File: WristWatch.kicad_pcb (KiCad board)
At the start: 4 copper layers, 32 x 32 mm, 86 parts, among them Q1 Q_PMOS_GSD, Q2 Q_PMOS_GSD, U2 STM32L412KBUx, U3 LIS2DE12, U4 AP2205-3.0, U5 MCP73832-2-OT, U6 ESP32-C3, Y1 32.768k

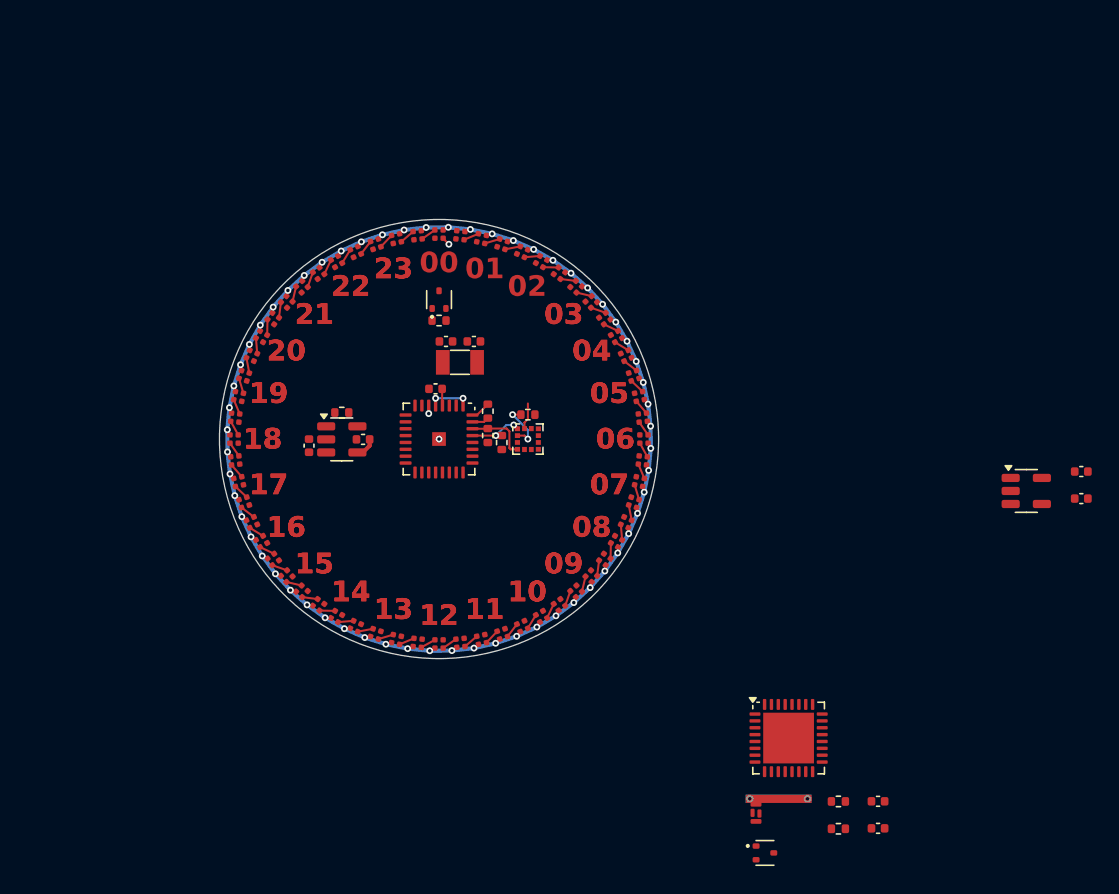
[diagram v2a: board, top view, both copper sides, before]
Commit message: This board is actually stupid. Moving on. Dual MCU architecture felt cool. It was in fact, overly complicated. Finally got the STM32F401 RTC to work. Fighting the L412 though.
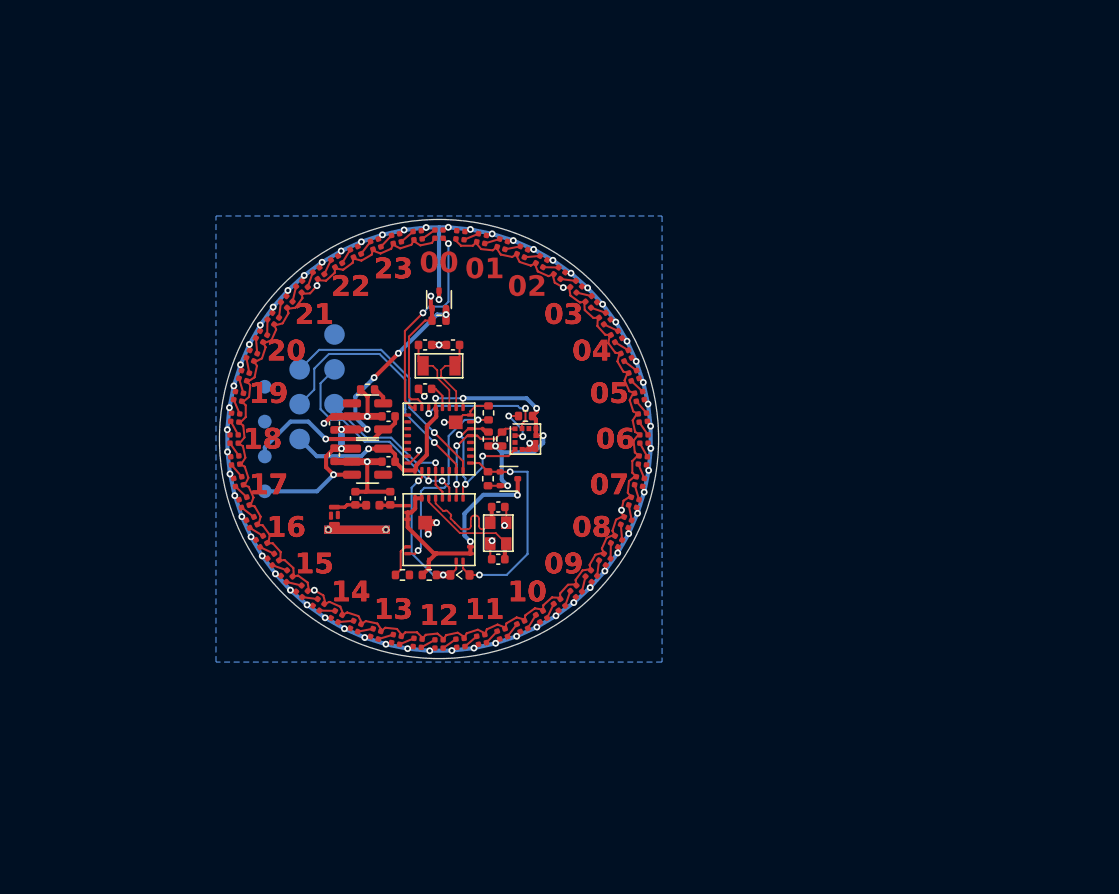
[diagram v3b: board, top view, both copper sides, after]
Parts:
- added C18: 1.8p, Capacitor_SMD:C_0402_1005Metric, F.Cu at (-3.56, 4.32)
- added C19: 1.2p, Capacitor_SMD:C_0402_1005Metric, F.Cu at (-6.10, 4.32)
- added D61: D, Diode_SMD:D_SOD-523, F.Cu at (1.52, 9.91)
- added J1: vcc, TestPoint:TestPoint_Pad_D1.0mm, B.Cu at (-12.7, 3.81)
- added J2: gnd, TestPoint:TestPoint_Pad_D1.0mm, B.Cu at (-12.7, -3.81)
- added J3: vcc, TestPoint:TestPoint_Pad_D1.0mm, B.Cu at (-12.7, 1.27)
- added J4: gnd, TestPoint:TestPoint_Pad_D1.0mm, B.Cu at (-12.7, -1.27)
- added L2: 3n, Inductor_SMD:L_0402_1005Metric, F.Cu at (-4.83, 4.83)
- added R13: 1M, Resistor_SMD:R_0402_1005Metric, F.Cu at (-0.71, 9.91)
- added TP1: ETX_SRX, TestPoint:TestPoint_Pad_D1.5mm, B.Cu at (-7.62, -2.54)
- added TP2: ERX_STX, TestPoint:TestPoint_Pad_D1.5mm, B.Cu at (-7.62, -5.08)
- added TP3: SWDIO, TestPoint:TestPoint_Pad_D1.5mm, B.Cu at (-10.2, -2.54)
- added TP4: SWCLK, TestPoint:TestPoint_Pad_D1.5mm, B.Cu at (-10.2, -5.08)
- added TP5: VCC, TestPoint:TestPoint_Pad_D1.5mm, B.Cu at (-10.2, 0.00)
- added TP6: GND, TestPoint:TestPoint_Pad_D1.5mm, B.Cu at (-7.62, -7.62)
- added Y2: 40M, Crystal:Crystal_SMD_2520-4Pin_2.5x2.0mm, F.Cu at (4.32, 6.86)
- AE1: moved to B.Cu
- moved C12 54.4 mm to (-7.62, 1.14), turned to -90 degrees
- moved C13 50.6 mm to (-3.68, 1.65), turned to 180 degrees
- moved U4 48.1 mm to (-5.21, 1.65)
- moved AE1 38.3 mm to (-7.62, 4.99)
- moved R12 36.8 mm to (-2.67, 9.91)
- moved C16 35.0 mm to (4.32, 4.95), turned to 180 degrees
- moved R11 34.7 mm to (3.57, 2.90), turned to -90 degrees
- moved C17 33.9 mm to (4.32, 8.76)
- moved Q2 33.0 mm to (5.09, 2.90)
- moved U6 29.7 mm to (0.00, 6.60)
- moved R10 2.52 mm to (-5.21, -3.61)
- moved U5 2.52 mm to (-5.21, -1.65)
- moved C14 2.50 mm to (-3.68, -1.65)
- moved C15 2.47 mm to (-7.62, -1.14)
- moved C4 1.55 mm to (1.02, -6.86)
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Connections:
- net Net-(U2-PC14) renamed /stm_xtal+
- net Net-(U2-PC15) renamed /stm_xtal-
- net Net-(U6-XTAL_N) renamed /esp_xtal+
- net Net-(U6-XTAL_P) renamed /esp_xtal-
- C1 pad 1: GND -> Net-(U2-NRST)
- C1 pad 2: Net-(U2-NRST) -> GND
- C12 pad 1: VCC -> +BATT
- Q1 pad 1: Net-(Q1-G) -> LED_PWR_EN
- R1 pad 1: GND -> STM_BOOT
- R1 pad 2: Net-(U2-PH3) -> GND
- R6 pad 1: Net-(Q1-G) -> LED_PWR_EN
- U2 pad 13: LED_IN -> unconnected-(U2-PA7-Pad13)
- U2 pad 18: unconnected-(U2-PA8-Pad18) -> ESP_BOOT
- U2 pad 19: unconnected-(U2-PA9-Pad19) -> ESP_RX
- U2 pad 20: unconnected-(U2-PA10-Pad20) -> ESP_TX
- U2 pad 23: unconnected-(U2-PA13-Pad23) -> SWDIO
- U2 pad 24: unconnected-(U2-PA14-Pad24) -> SWCLK
- U2 pad 25: unconnected-(U2-PA15-Pad25) -> ESP_PWR_EN
- U2 pad 31: Net-(U2-PH3) -> STM_BOOT
- U2 pad 7: unconnected-(U2-PA1-Pad7) -> LED_PWR_EN
- U2 pad 8: unconnected-(U2-PA2-Pad8) -> LED_IN
- U4 pad 1: VCC -> +BATT
- U4 pad 3: VCC -> +BATT
- U6 pad 1: Net-(AE1-A) -> Net-(U6-LNA_IN)
- U6 pad 15: BOOT -> ESP_BOOT
- U6 pad 16: unconnected-(U6-GPIO10-Pad16) -> ESP_PWR_EN
- U6 pad 8: unconnected-(U6-GPIO3-Pad8) -> STM_BOOT
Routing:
- net GND: track 1.45 -> 142.6 mm, vias 1 -> 16
- net +3V0: track 3.07 -> 37.4 mm, vias 2 -> 7
- net +BATT: track 0.00 -> 29.7 mm, vias 0 -> 7
- net /ESP_VDD: track 0.00 -> 19.1 mm, vias 0 -> 2
- net SWDIO: track 0.00 -> 19.0 mm, vias 0 -> 1
- net SWCLK: track 0.00 -> 17.8 mm, vias 0 -> 1
- net ESP_PWR_EN: track 0.00 -> 16.5 mm, vias 0 -> 2
- net ESP_RX: track 0.00 -> 16.3 mm, vias 0 -> 2
- net STM_BOOT: track 0.00 -> 15.0 mm, vias 0 -> 2
- net LED_IN: track 0.61 -> 14.9 mm, vias 1 -> 2
- net ESP_BOOT: track 0.00 -> 12.6 mm, vias 0 -> 2
- net ESP_TX: track 0.00 -> 11.7 mm, vias 0 -> 1
- net VBUS: track 1.55 -> 12.4 mm, vias 0 -> 1
- net LED_PWR_EN: track 0.00 -> 9.85 mm, vias 0 -> 1
- net /esp_xtal-: track 0.00 -> 8.36 mm
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- added copper zone on B.Cu, net GND
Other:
- copper layers 4 -> 2
- board text added: "BATT"
- board text added: "EEAN"
- board text added: "ERX SCK"
- board text added: "ETX DIO"
- board text added: "GND"
- board text added: "VBUS"
- board text added: "VCC"

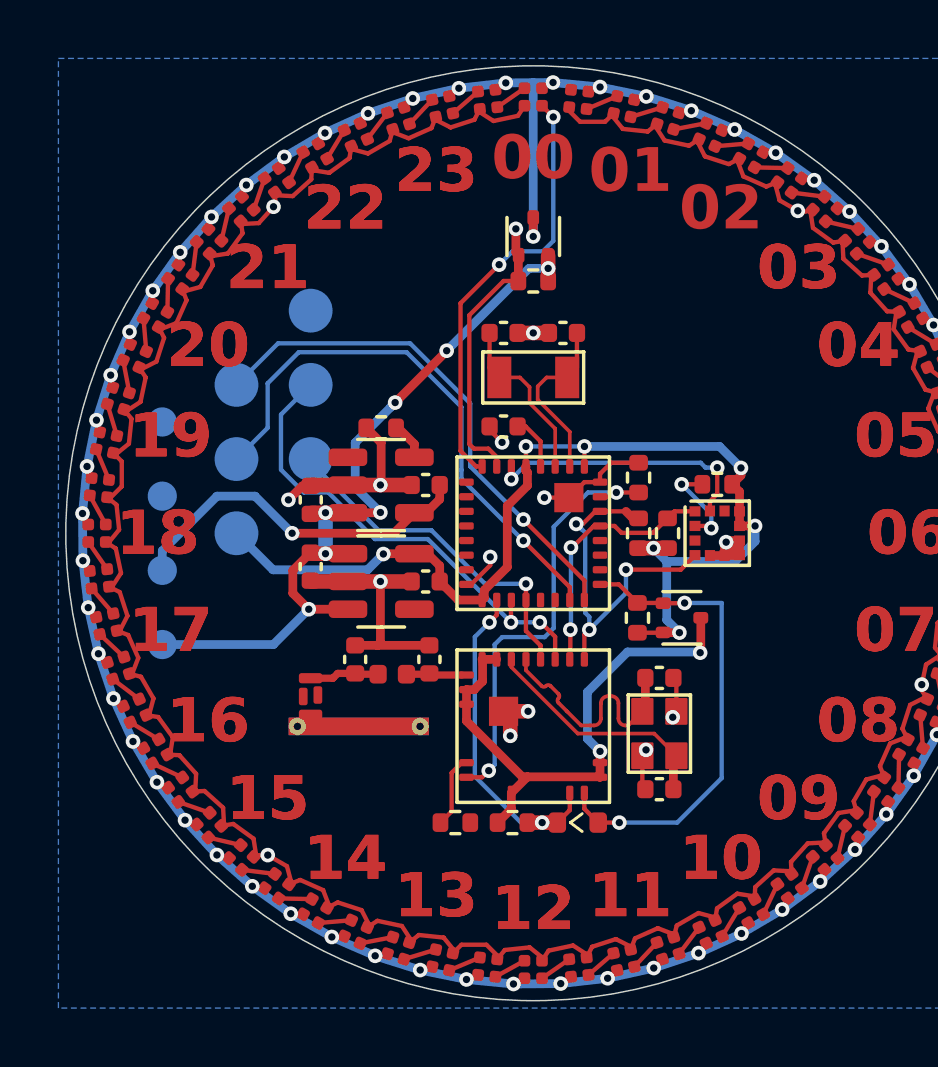
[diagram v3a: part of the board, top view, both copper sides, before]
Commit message: A much more reasonable architecture
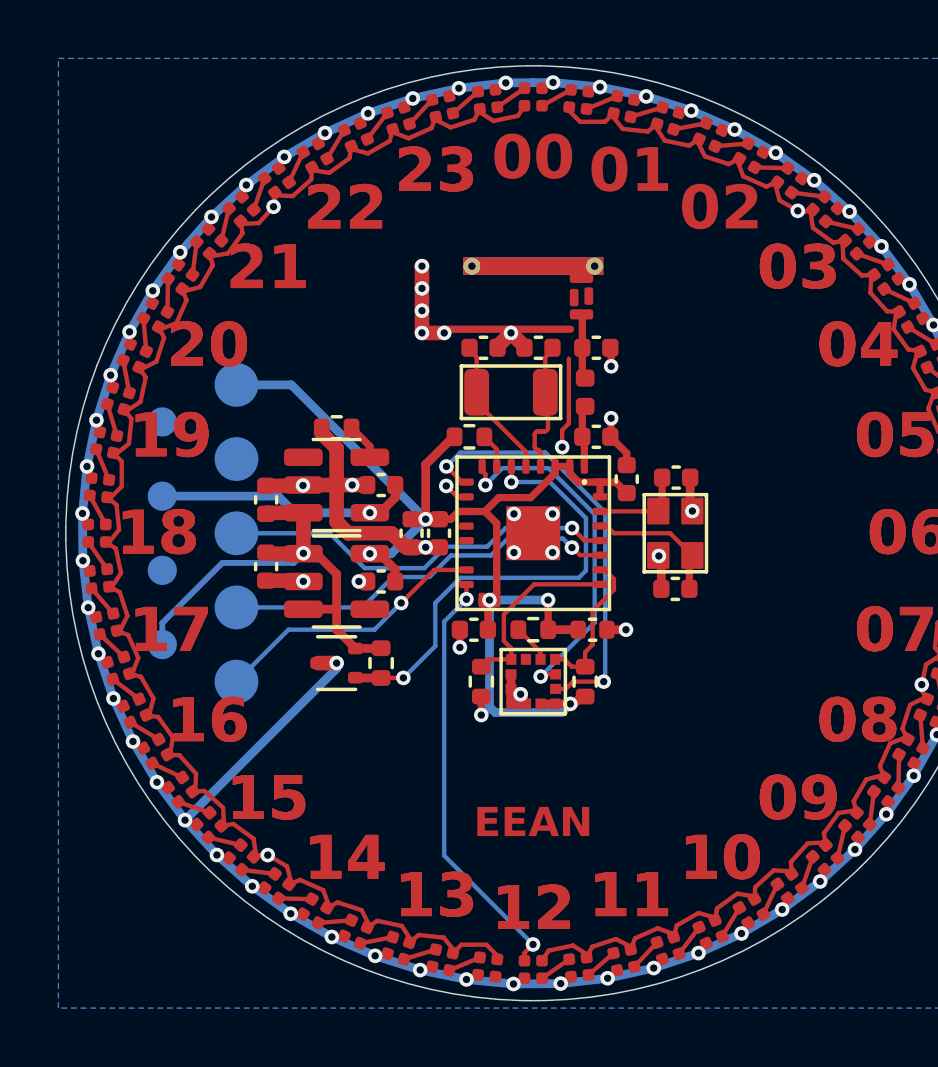
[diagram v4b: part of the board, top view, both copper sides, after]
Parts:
- removed D61: D, Diode_SMD:D_SOD-523
- removed Q2: Q_PMOS_GSD, Package_TO_SOT_SMD:SOT-523
- removed R1: 10k, Resistor_SMD:R_0402_1005Metric
- removed R11, R13: 1M, Resistor_SMD:R_0402_1005Metric
- removed TP4: SWCLK, TestPoint:TestPoint_Pad_D1.5mm
- removed U2: STM32L412KBUx, Package_DFN_QFN:QFN-32-1EP_5x5mm_P0.5mm_EP3.45x3.45mm
- removed Y1: 32.768k, Crystal:Crystal_SMD_3215-2Pin_3.2x1.5mm
- added C20: 100n, Capacitor_SMD:C_0402_1005Metric, F.Cu at (3.20, -1.85)
- added C21: 100n, Capacitor_SMD:C_0402_1005Metric, F.Cu at (-2.03, 3.30)
- added C21: 100n, Capacitor_SMD:C_0402_1005Metric, F.Cu at (2.03, 3.30)
- added C22: 100n, Capacitor_SMD:C_0402_1005Metric, F.Cu at (-3.23, 0.00)
- added Y3: 32.768k, Crystal:Crystal_SMD_EuroQuartz_EQ161-2Pin_3.2x1.5mm, F.Cu at (-0.76, -4.83)
- C1: value 100n -> 12p
- C17: value 12p -> 10u
- C4, C7: value 4p3 -> 12p
- R6: value 1M -> 100k
- TP1: value ETX_SRX -> TX
- TP2: value ERX_STX -> RX
- TP3: value SWDIO -> BOOT
- moved Q1 16.1 mm to (-6.73, 4.45), turned to 180 degrees
- moved AE1 16.1 mm to (0.00, -9.14), turned to 180 degrees
- moved R6 14.1 mm to (-5.21, 4.45), turned to 90 degrees
- moved C19 13.5 mm to (2.16, -6.35), turned to 0 degrees
- moved R12 13.2 mm to (-2.18, -3.30), turned to 180 degrees
- moved C17 12.2 mm to (-4.17, 0.00), turned to -90 degrees
- moved L2 11.7 mm to (1.78, -4.83), turned to 90 degrees
- moved C7 10.6 mm to (4.86, 1.91), turned to 0 degrees
- moved C18 9.52 mm to (2.16, -3.30), turned to 0 degrees
- moved U3 8.09 mm to (0.00, 5.08), turned to -90 degrees
- moved TP2 8.03 mm to (-10.2, 2.54)
- moved R9 8.03 mm to (0.00, 3.30)
- moved TP3 7.62 mm to (-10.2, 5.08)
- moved R8 7.40 mm to (-1.78, 5.08)
- moved C16 6.88 mm to (4.89, -1.91)
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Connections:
- C1 pad 1: Net-(U2-NRST) -> GND
- C1 pad 2: GND -> /xtl_ls+
- C16 pad 2: /esp_xtal+ -> /xtl_hs-
- C17 pad 1: GND -> +3V0
- C17 pad 2: /esp_xtal- -> GND
- C4 pad 2: /stm_xtal+ -> /xtl_ls-
- C7 pad 2: /stm_xtal- -> /xtl_hs+
- D1 pad 4: LED_IN -> Bank1
- D15 pad 2: Bank1 -> Bank2
- D16 pad 4: Bank1 -> Bank2
- D30 pad 2: Bank2 -> unconnected-(D30-DOUT-Pad2)
- D31 pad 4: Bank2 -> LED_DATA
- D60 pad 2: unconnected-(D60-DOUT-Pad2) -> Bank1
- R12 pad 2: /ESP_VDD -> +3V0
- TP3 pad 1: SWDIO -> ESP_BOOT
- U3 pad 11: IMU_INT2 -> IMU_SPAR_INT
- U3 pad 12: WKUP1 -> IMU_MOVE_INT
- U6 pad 11: /ESP_VDD -> +3V0
- U6 pad 16: ESP_PWR_EN -> LED_DATA
- U6 pad 17: /ESP_VDD -> +3V0
- U6 pad 18: /ESP_VDD -> +3V0
- U6 pad 2: /ESP_VDD -> +3V0
- U6 pad 29: /esp_xtal+ -> /xtl_hs+
- U6 pad 3: /ESP_VDD -> +3V0
- U6 pad 30: /esp_xtal- -> /xtl_hs-
- U6 pad 31: /ESP_VDD -> +3V0
- U6 pad 32: /ESP_VDD -> +3V0
- U6 pad 8: STM_BOOT -> IMU_MOVE_INT
- Y2 pad 1: /esp_xtal- -> /xtl_hs-
- Y2 pad 3: /esp_xtal+ -> /xtl_hs+
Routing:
- net /ESP_VDD: track 19.1 -> 0.00 mm, vias 2 -> 0
- net SWDIO: track 19.0 -> 0.00 mm, vias 1 -> 0
- net SWCLK: track 17.8 -> 0.00 mm, vias 1 -> 0
- net ESP_PWR_EN: track 16.5 -> 0.00 mm, vias 2 -> 0
- net STM_BOOT: track 15.0 -> 0.00 mm, vias 2 -> 0
- net IMU_SPAR_INT: track 0.00 -> 15.0 mm, vias 0 -> 2
- net LED_IN: track 14.9 -> 0.00 mm, vias 2 -> 0
- net LED_DATA: track 0.00 -> 14.6 mm, vias 0 -> 2
- net +BATT: track 29.7 -> 17.1 mm, vias 7 -> 1
- net IMU_MOVE_INT: track 0.00 -> 12.2 mm, vias 0 -> 2
- net WKUP1: track 9.52 -> 0.00 mm, vias 2 -> 0
- net /esp_xtal-: track 8.36 -> 0.00 mm
- net /esp_xtal+: track 8.31 -> 0.00 mm
- net +3V0: track 37.4 -> 44.5 mm, vias 7 -> 6
- net /stm_xtal+: track 6.00 -> 0.00 mm
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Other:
- board text removed: "BATT"
- board text removed: "ERX SCK"
- board text removed: "ETX DIO"
- board text removed: "GND"
- board text removed: "VBUS"
- board text removed: "VCC"
